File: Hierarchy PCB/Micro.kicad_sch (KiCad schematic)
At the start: 2 parts, among them U9 STM32L476RGTx

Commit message: Add files via upload
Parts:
- added C14: 1 uF, symbol Device:C
- added C15: .01 uF, symbol Device:C
- added C16: 4.7 uF, symbol Device:C
- added C17, C18, C19, C20: .1 uF, symbol Device:C
- added FB1, FB2: FerriteBead, symbol Device:FerriteBead
- added J5, J6, J7, J8: Programming Pin, symbol Connector_Generic_MountingPin:Conn_01x01_MountingPin
- added U11: MAX7375AXR805, Package_TO_SOT_SMD:SOT-323_SC-70, symbol Oscillator:MAX7375AXR805
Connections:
- net +3.3 VD: now reaches FB3.1
- net +3.3 VD: now also U9.1 (VBAT), U9.18 (VSS), U9.19 (VDD), U9.31 (VSS), U9.32 (VDD), U9.47 (VSS), U9.48 (VDDUSB), U9.63 (VSS), U9.64 (VDD), C16.1, C16.2, C17.1, C17.2, C18.1, C18.2, C19.1, C19.2, C20.1, C20.2, FB1.1, FB2.2, U11.1 (V+), U11.3 (GND)
- net at FB3.2: now also C14.1, C15.1; no longer U9.13 (VDDA)
- net at U9.12 (VSSA): now also FB2.1
- net GPS Chip RX (Pin 10): now reaches U9.14 (PA0)
- net GPS Chip TX (Pin 9): now reaches U9.15 (PA1)
- net DAC Output 1 (Electrical signals to Amplifier): now reaches U9.20 (PA4)
- net at U9.46 (PA13): now also J5.1 (Pin_1)
- net at U9.49 (PA14): now also J6.1 (Pin_1)
- net at U9.5 (PH0): now also U11.2 (CLOCK)
- net LoRa Chip RXD (Pin 3): now reaches U9.53 (PC12)
- net LoRa Chip TXD (Pin 4): now reaches U9.54 (PD2)
- net at U9.60 (BOOT0): now also J7.1 (Pin_1)
- net at U9.7 (NRST): now also J8.1 (Pin_1)
- new net: C14.2, C15.2, FB1.2
- no-connect marks 0 -> 43
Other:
- note added: "3VA"
- note added: "Coupling Capacitors"
- moved on the sheet: FB3, U9

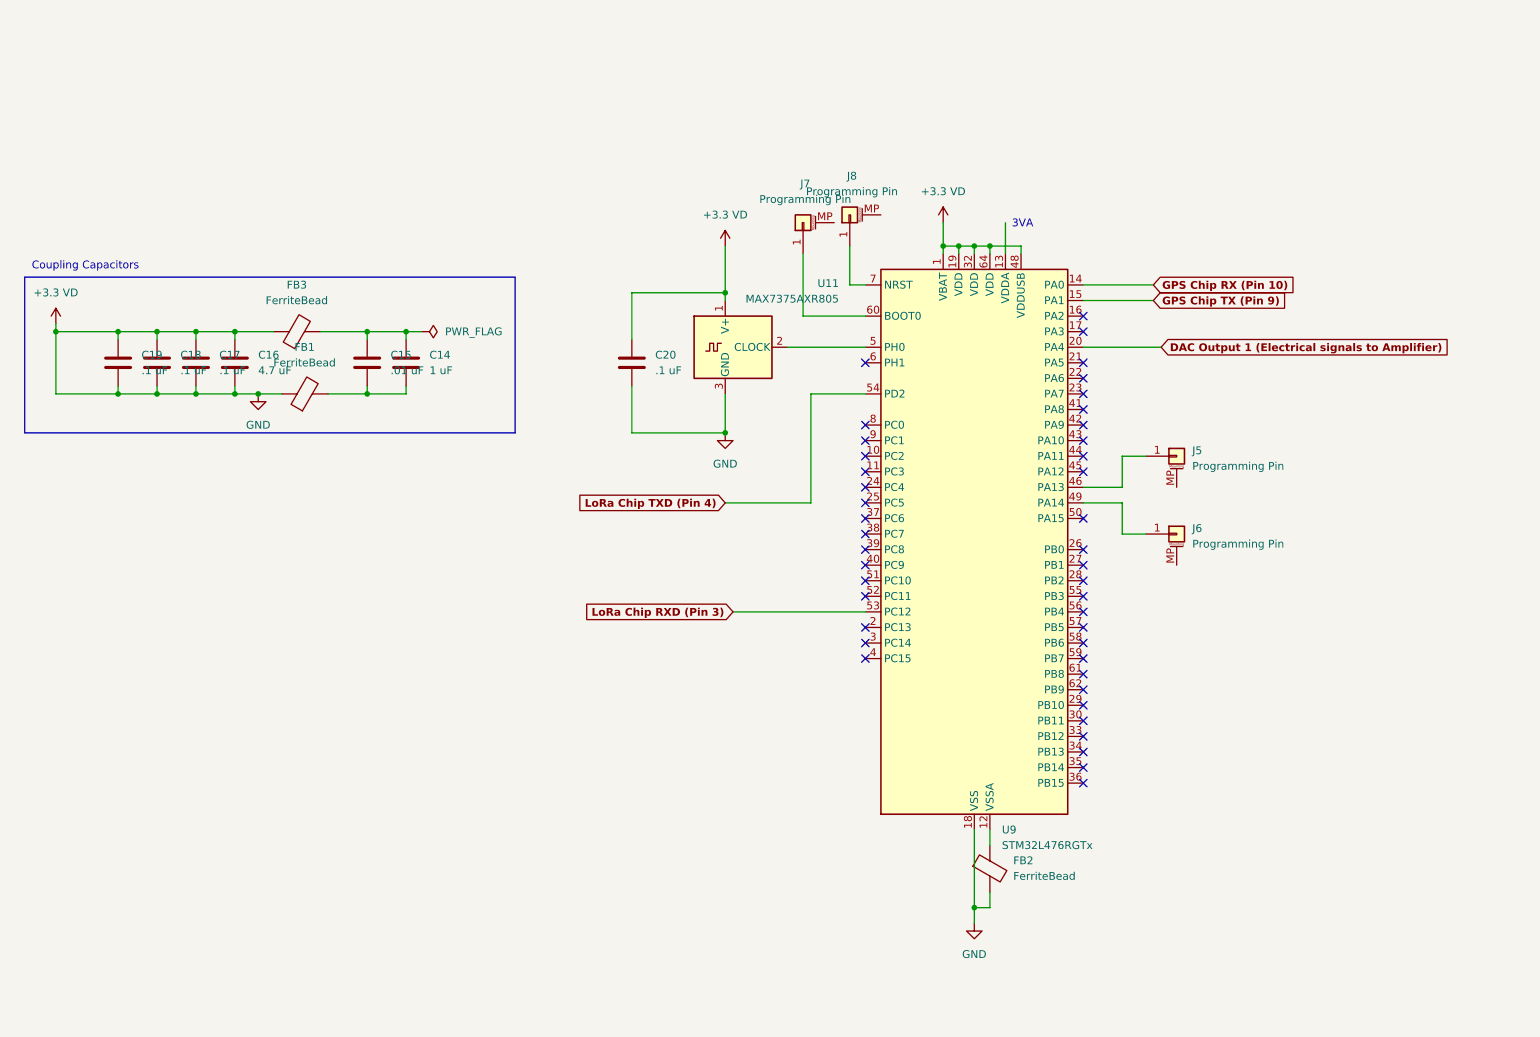
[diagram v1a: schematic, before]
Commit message: Updated Micro in hieracrchy
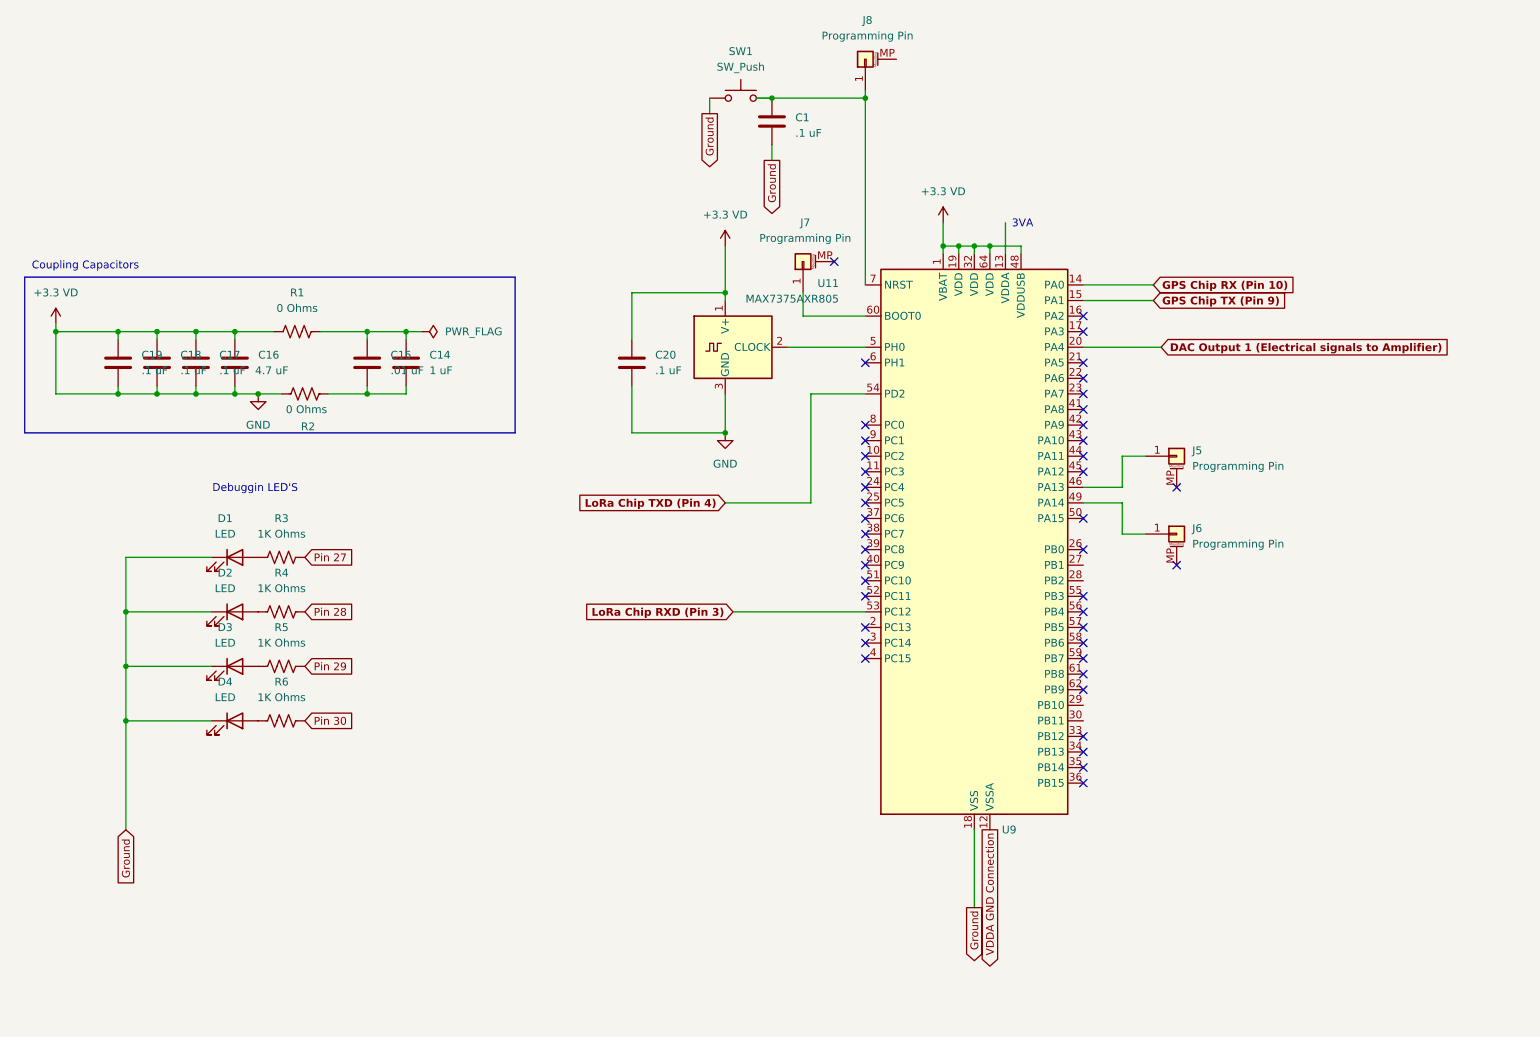
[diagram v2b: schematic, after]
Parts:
- removed FB1, FB2, FB3: FerriteBead, symbol Device:FerriteBead
- added C1: .1 uF, Capacitor_SMD:C_0805_2012Metric_Pad1.18x1.45mm_HandSolder, symbol Device:C
- added D1, D2, D3, D4: LED, LED_SMD:LED_0805_2012Metric, symbol Device:LED
- added R1, R2: 0 Ohms, symbol Device:R_US
- added R3, R4, R5, R6: 1K Ohms, Resistor_SMD:R_0805_2012Metric, symbol Device:R_US
- added SW1: SW_Push, Button_Switch_THT:SW_PUSH_6mm_H5mm, symbol Switch:SW_Push
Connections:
- net +3.3 VD: now also R1.1, R2.1; no longer U9.18 (VSS), U9.31 (VSS), U9.47 (VSS), U9.63 (VSS)
- net at C14.2, C15.2: now also R2.2
- net VDDA GND Connection: now reaches U9.12 (VSSA)
- net at C14.1, C15.1: now also R1.2
- net at J8.1 (Pin_1), U9.7 (NRST): now also C1.1, SW1.2
- new net: D4.2 (A), R6.1
- new net: D1.2 (A), R3.1
- new net: D2.2 (A), R4.1
- new net: D3.2 (A), R5.1
- new net Ground: C1.2, D1.1 (K), D2.1 (K), D3.1 (K), D4.1 (K), SW1.1, U9.18 (VSS), U9.31 (VSS), U9.47 (VSS), U9.63 (VSS)
- new net Pin 27: R3.2
- new net Pin 28: R4.2
- new net Pin 29: R5.2
- new net Pin 30: R6.2
- no-connect marks 43 -> 42
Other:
- note added: "Debuggin LED'S"
- moved on the sheet: J7, J8

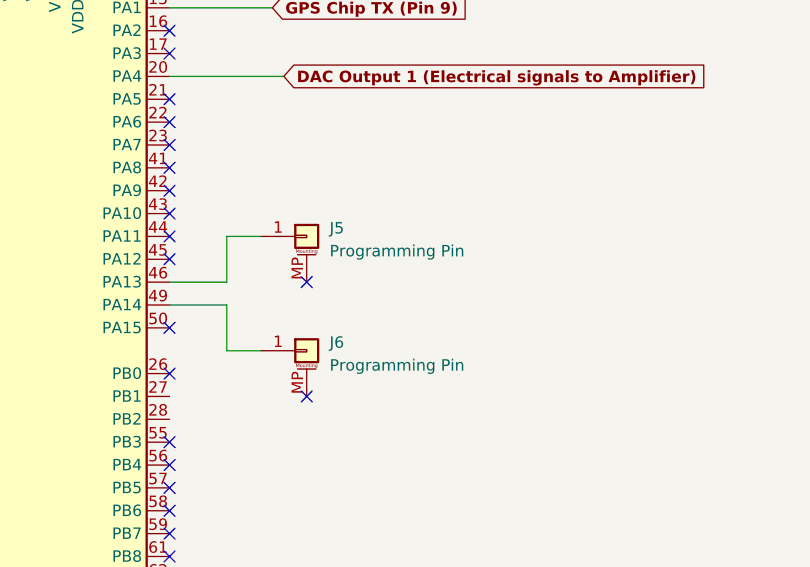
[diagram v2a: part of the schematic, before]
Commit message: updated micro hierarachy slightly
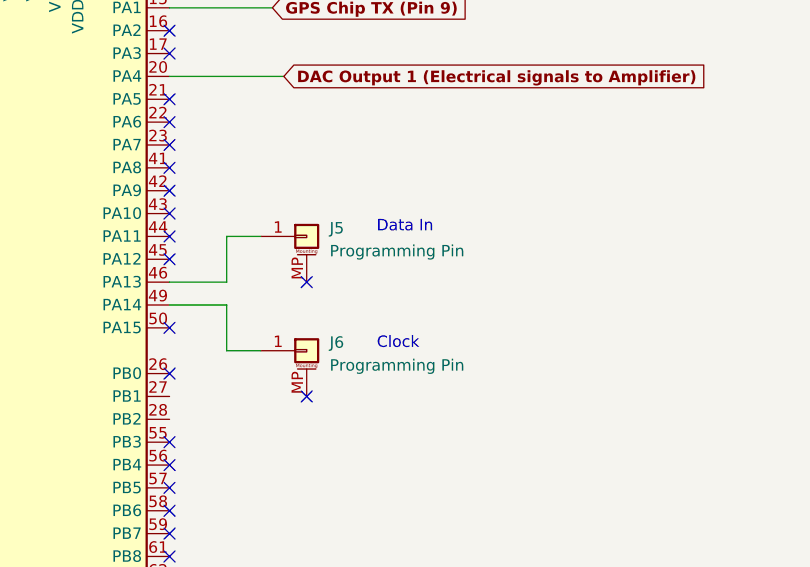
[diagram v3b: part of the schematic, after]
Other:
- note added: "Clock"
- note added: "Data In"
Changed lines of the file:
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@@
+		)
+	)
+	(text "Clock\n"
+		(exclude_from_sim no)
+		(at 240.03 94.488 0)
+		(effects
+			(font
+				(size 1.27 1.27)
+			)
 		)
 	)
@@
 		(effects
 			(font
+				(size 1.27 1.27)
+			)
+		)
+	)
+	(text "Data In"
+		(exclude_from_sim no)
+		(at 240.792 81.534 0)
+		(effects
+			(font
